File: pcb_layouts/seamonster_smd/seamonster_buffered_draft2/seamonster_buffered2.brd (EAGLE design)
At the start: 172.5 x 106.5 mm, 125 parts, among them IC1 7808DT, IC2 4051D, IC3 4051D, IC4 DG408DY, IC5 4046D, IC6 40106D, IC7 4070D, IC8 4046D, IC9 4040D, Q1 THONKICONNNEW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

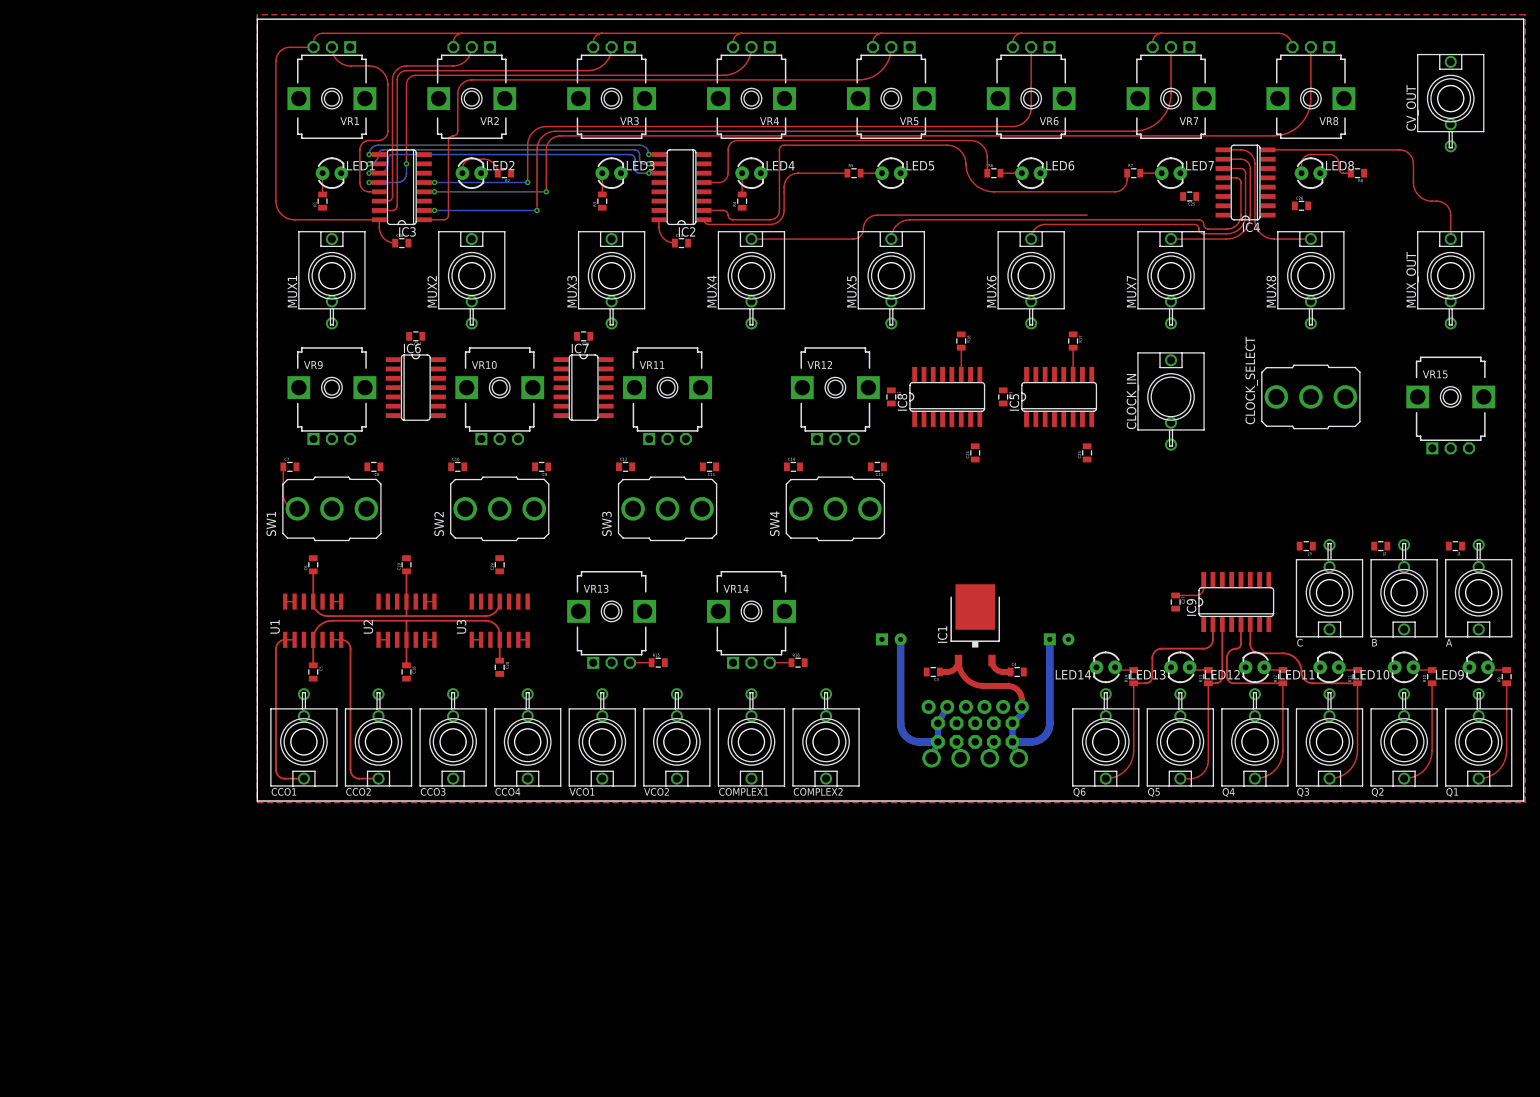
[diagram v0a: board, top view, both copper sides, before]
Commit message: made and custom part for 8 way Alpha rotary switch as clock speed selector
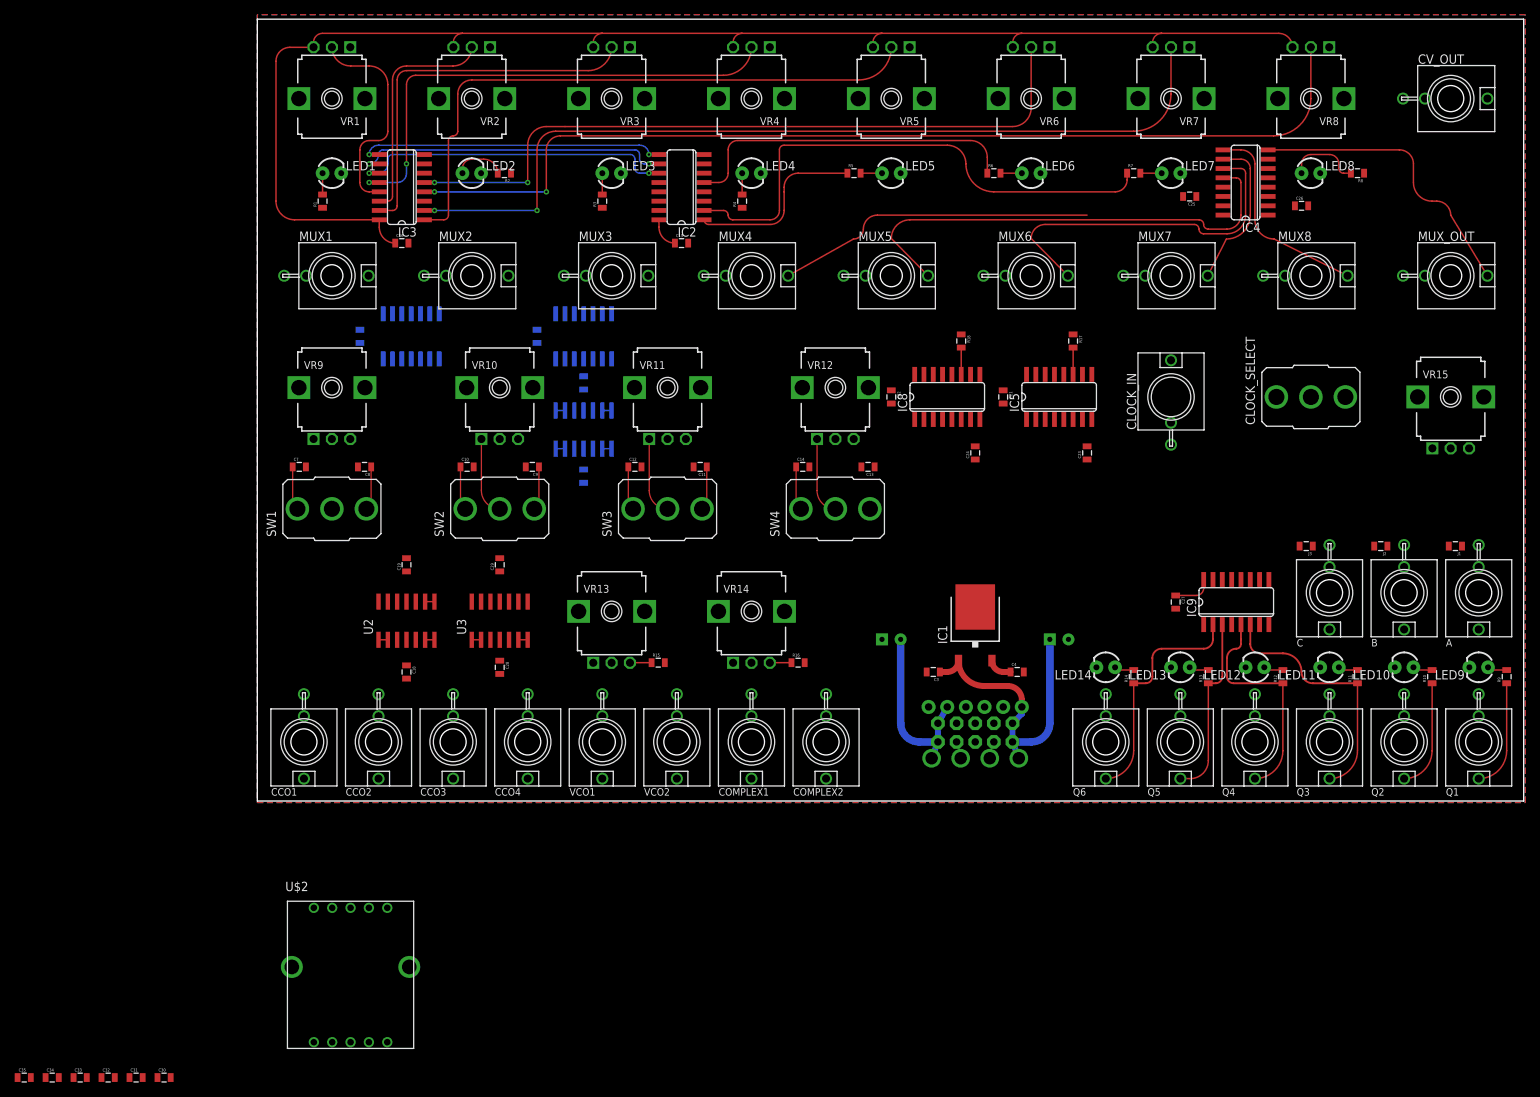
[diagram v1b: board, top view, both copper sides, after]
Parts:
- added C30, C31, C32, C33, C34, C35: (no value), SparkFun-Capacitors:0805
- added U$2: ALPHA_ROTARY_SWITCH, alpha_8pos_rotary_switch:ALPHA_SR1712F
- moved C5 45.5 mm to (44.5, 55.2), flipped to the bottom
- moved U1 45.1 mm to (44.5, 61.6), flipped to the bottom
- moved C6 44.4 mm to (44.5, 67.9), flipped to the bottom
- moved C20 30.5 mm to (14.0, 74.3), flipped to the bottom, turned to 90 degrees
- moved IC7 24.5 mm to (21.0, 74.3), flipped to the bottom, turned to 180 degrees
- moved IC6 23.9 mm to (44.5, 74.3), flipped to the bottom, turned to 180 degrees
- moved C17 16.5 mm to (38.1, 74.3), flipped to the bottom, turned to 90 degrees
- moved C12 1.27 mm to (51.4, 56.5)
- moved C10 1.27 mm to (28.6, 56.5)
- moved C7 1.27 mm to (5.71, 56.5)
- moved C8 1.27 mm to (14.6, 56.5)
- moved C11 1.27 mm to (60.3, 56.5)
- moved C13 1.27 mm to (83.2, 56.5)
- moved C14 1.27 mm to (74.3, 56.5)
- moved C9 1.27 mm to (37.5, 56.5)
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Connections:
- net CCO1 renamed INV_B_OUT
- net N$46 renamed INV_B_IN
- net N$53 renamed INV_C_IN
- net N$54 renamed INV_C_OUT
- net N$57 renamed INV_D_OUT
- net N$58 renamed INV_D_IN
- net N$61 renamed INV_E_OUT
- net N$62 renamed INV_E_IN
- removed net N$41: IC6.1, VR15.1
- new net N$2: IC6.1, U$2.1, U$2.10, VR15.1
- new net N$3: C30.1, U$2.2
- new net N$4: C31.1, U$2.3
- new net N$5: C32.1, U$2.4
- new net N$6: C33.1, U$2.5
- new net N$7: C34.1, U$2.6
- new net N$8: C35.1, U$2.7
- net GND: now also C30.2, C31.2, C32.2, C33.2, C34.2, C35.2
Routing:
- net V+: track 80.6 -> 40.2 mm
- net V-: track 62.3 -> 25.0 mm
- net CCO2_BUFFERED: track 23.8 -> 1.27 mm
- net CCO1_BUFFERED: track 23.8 -> 1.27 mm
- net INV_C_IN: track 0.00 -> 10.5 mm
- net INV_E_IN: track 0.00 -> 10.5 mm
- net INV_D_IN: track 0.00 -> 10.5 mm
- net MUX5: track 57.2 -> 64.3 mm
- net MUX6: track 40.7 -> 47.8 mm
- net N$1: track 33.3 -> 39.7 mm
- net MUX8: track 21.5 -> 27.6 mm
- net N$63: track 0.00 -> 5.98 mm
- net N$60: track 0.00 -> 5.98 mm
- net N$59: track 0.00 -> 5.98 mm
- net N$56: track 0.00 -> 5.98 mm
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
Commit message: routed power nets, moved ICs
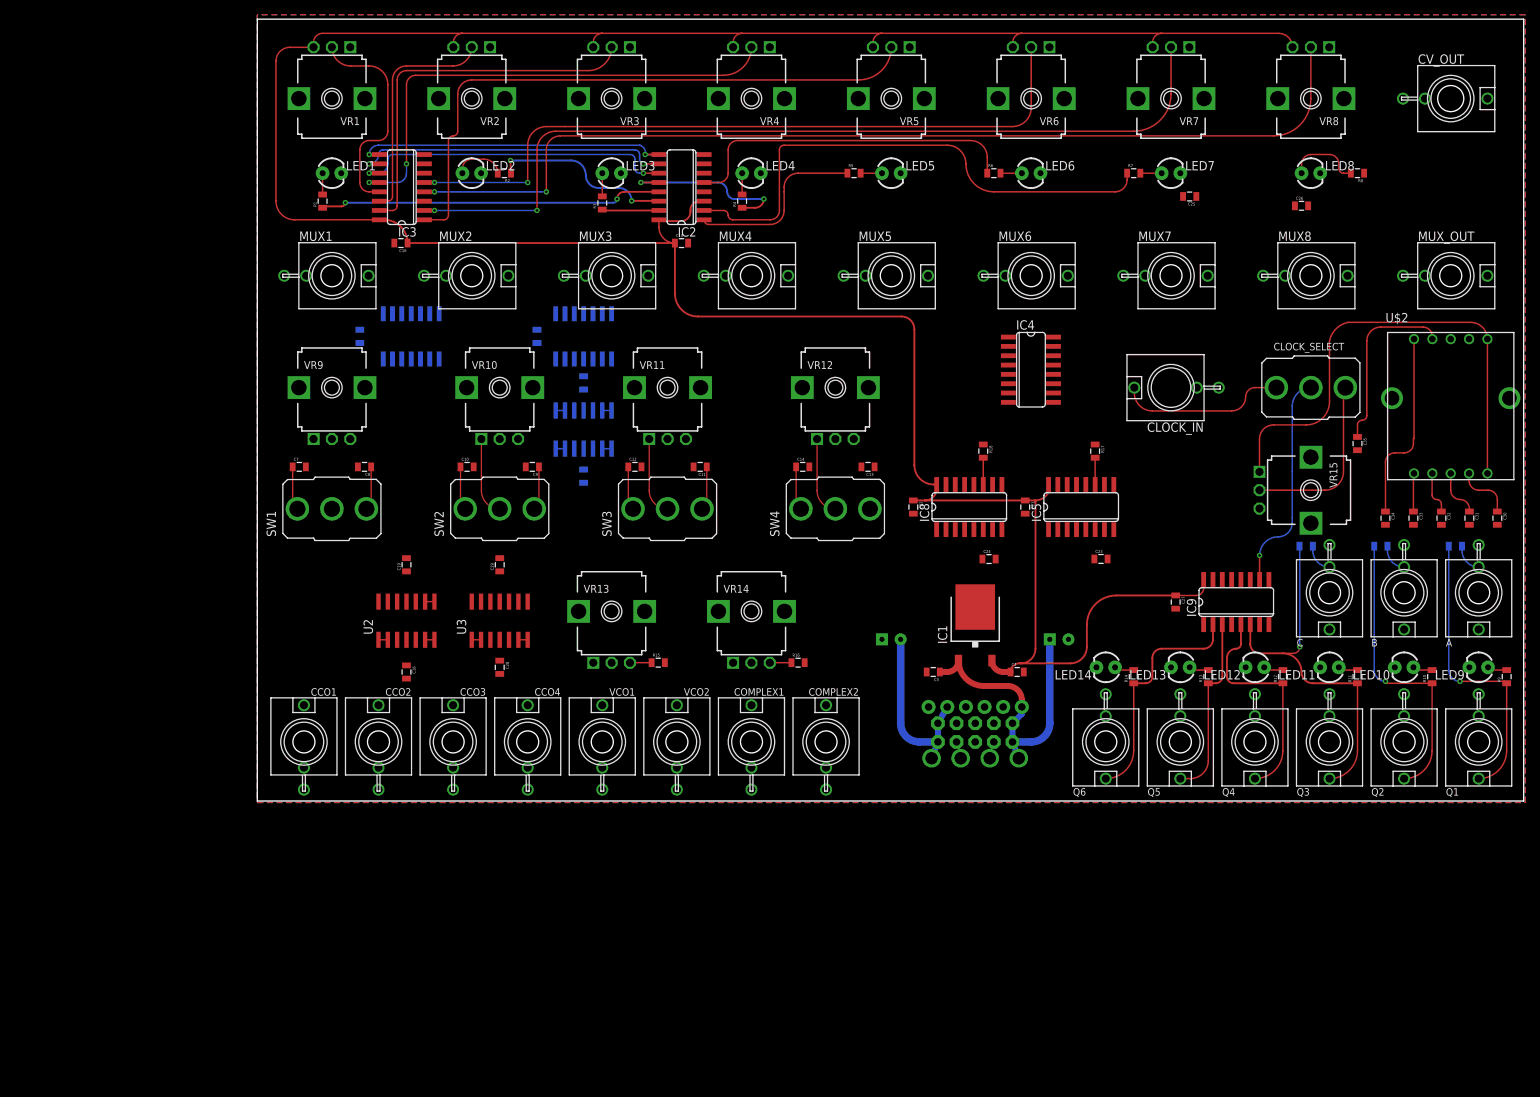
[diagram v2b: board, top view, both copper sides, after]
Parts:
- moved C35 201.1 mm to (149.9, 59.7), turned to 270 degrees
- moved C30 196.9 mm to (168.9, 49.5), turned to 270 degrees
- moved C31 196.9 mm to (165.1, 49.5), turned to 270 degrees
- moved C32 196.9 mm to (161.3, 49.5), turned to 270 degrees
- moved C33 196.9 mm to (157.5, 49.5), turned to 270 degrees
- moved C34 196.9 mm to (153.7, 49.5), turned to 270 degrees
- moved U$2 168.7 mm to (162.6, 64.8)
- moved IC4 38.8 mm to (105.4, 69.8), turned to 270 degrees
- moved VR15 22.9 mm to (143.5, 53.3), turned to 270 degrees
- moved C21 15.3 mm to (104.6, 51.0)
- moved C22 15.3 mm to (89.4, 51.0)
- moved IC5 15.3 mm to (112.2, 51.0)
- moved IC8 15.3 mm to (97.0, 51.0)
- moved R17 15.3 mm to (114.1, 58.7)
- moved R18 15.3 mm to (98.9, 58.7)
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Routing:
- net VCC: track 206.5 -> 389.9 mm
- net N$2: track 0.00 -> 65.9 mm
- net MUX5: track 64.3 -> 0.00 mm
- net MUX6: track 47.8 -> 0.00 mm
- net N$19: track 0.00 -> 46.7 mm, vias 0 -> 2
- net MUX4: track 43.4 -> 0.00 mm
- net N$1: track 39.7 -> 0.00 mm
- net N$50: track 0.00 -> 29.0 mm, vias 0 -> 1
- net MUX8: track 27.6 -> 0.00 mm
- net N$7: track 0.00 -> 25.8 mm
- net Q2: track 14.6 -> 40.1 mm, vias 0 -> 1
- net Q1: track 14.6 -> 40.1 mm, vias 0 -> 1
- net N$20: track 0.00 -> 24.3 mm, vias 0 -> 2
- net N$8: track 0.00 -> 24.2 mm
- net N$43: track 0.00 -> 24.0 mm
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
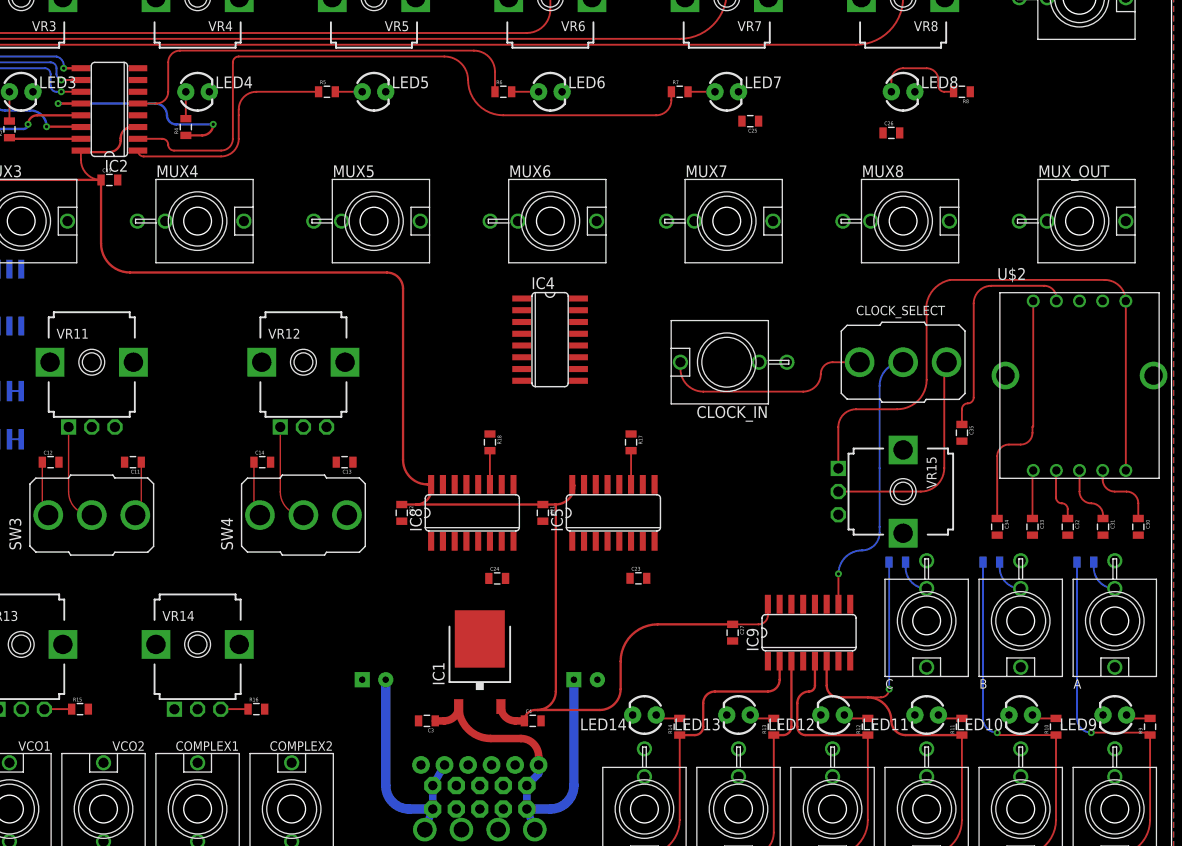
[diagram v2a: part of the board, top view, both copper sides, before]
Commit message: routed 408 MUX power and most IO
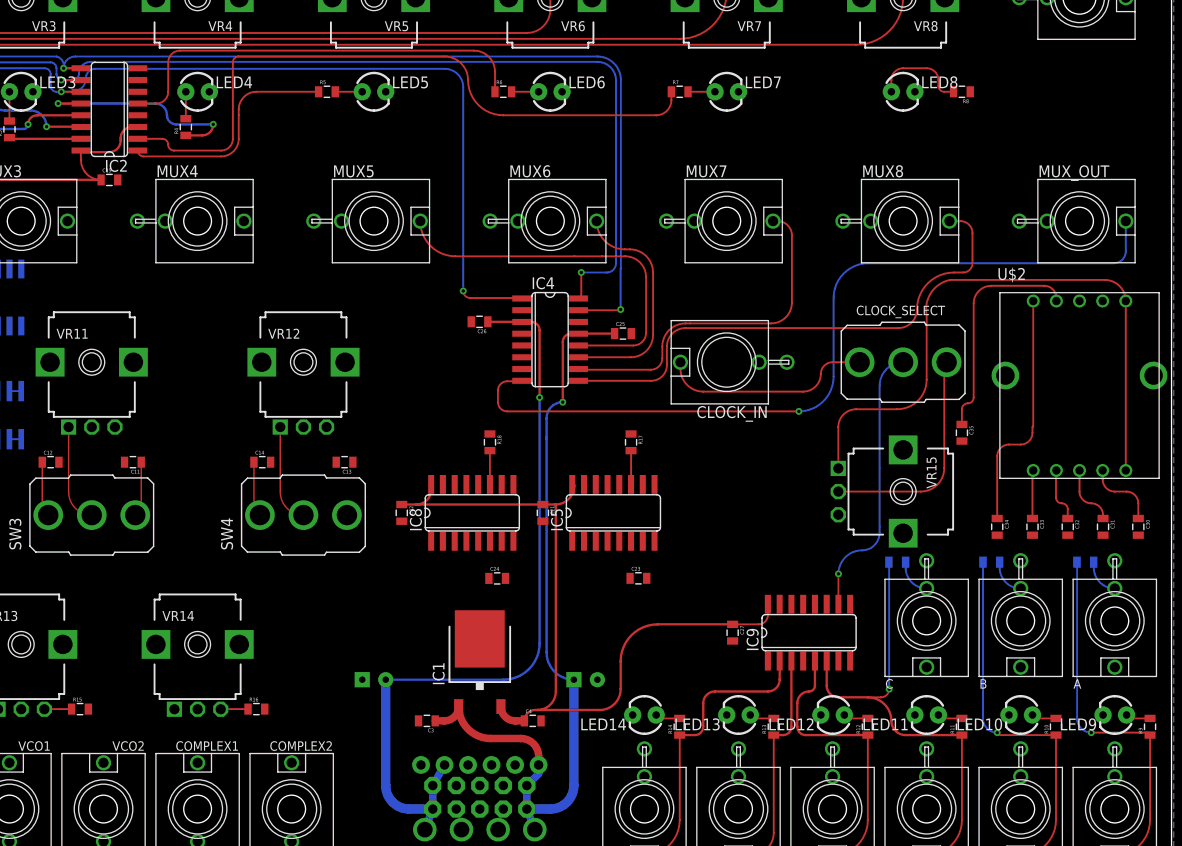
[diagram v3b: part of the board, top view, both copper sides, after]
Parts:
- moved C26 48.9 mm to (97.8, 71.7), turned to 180 degrees
- moved C25 26.7 mm to (113.2, 70.4), turned to 0 degrees
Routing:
- net C: track 43.9 -> 133.2 mm, vias 2 -> 3
- net B: track 43.0 -> 131.9 mm, vias 2 -> 3
- net N$1: track 0.00 -> 87.9 mm, vias 0 -> 1
- net A: track 44.1 -> 118.0 mm, vias 2 -> 3
- net VCC: track 389.9 -> 325.8 mm
- net V-: track 25.0 -> 83.1 mm, vias 0 -> 1
- net MUX8: track 0.00 -> 55.3 mm
- net V+: track 40.2 -> 84.9 mm, vias 0 -> 1
- net MUX5: track 0.00 -> 40.8 mm
- net MUX7: track 0.00 -> 36.7 mm
- net MUX6: track 0.00 -> 24.2 mm
